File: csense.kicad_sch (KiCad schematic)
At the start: 28 parts, among them U4 NCS214

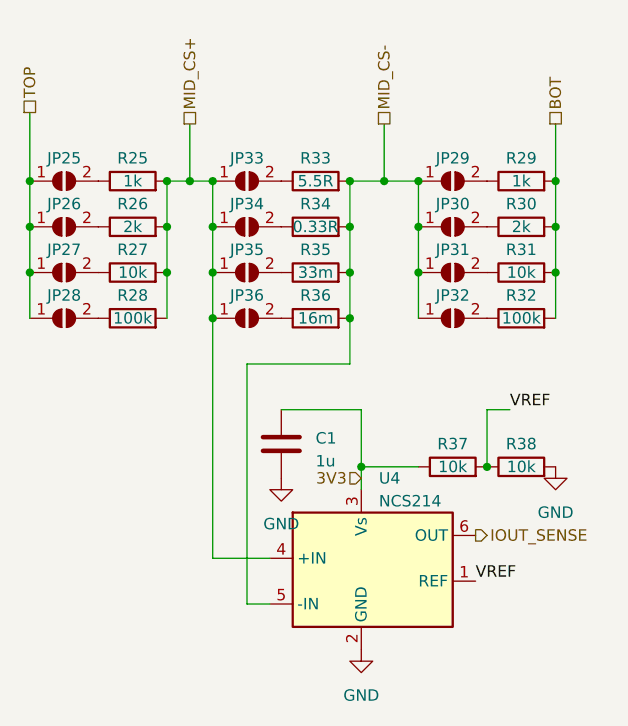
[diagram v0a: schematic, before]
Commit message: Build pogoplayground v1.0 - Fix continuity tester reference voltage - Fix SSR 5V supply
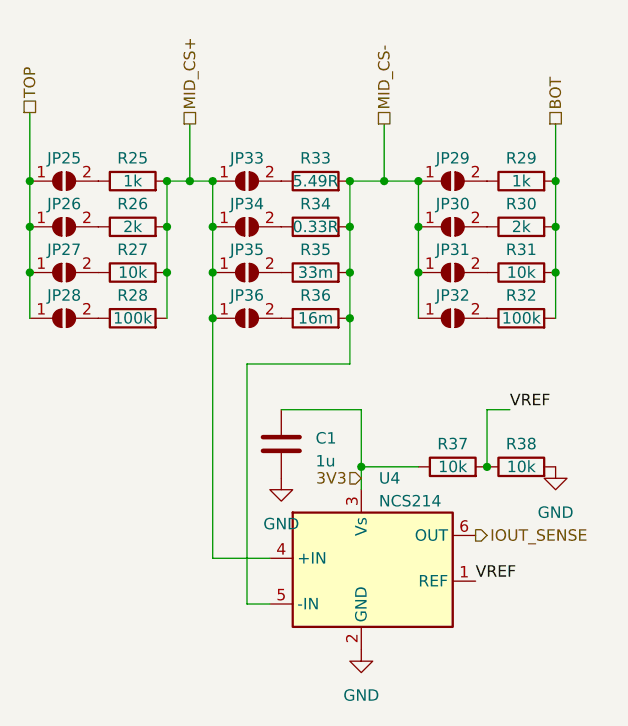
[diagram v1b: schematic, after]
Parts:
- R33: value 5.5R -> 5.49R
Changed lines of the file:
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@@
       (effects (font (size 1.27 1.27)))
     )
-    (property "Value" "5.5R" (at 72.39 40.64 90)
+    (property "Value" "5.49R" (at 72.39 40.64 90)
       (effects (font (size 1.27 1.27)))
     )
